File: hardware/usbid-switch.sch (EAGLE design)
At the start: 5 parts, among them J1 USB-MICRO-ZX80-B-5S, J2 USB-MICRO-105133-0011, SW1 SWITCH-SPDT-EG1215

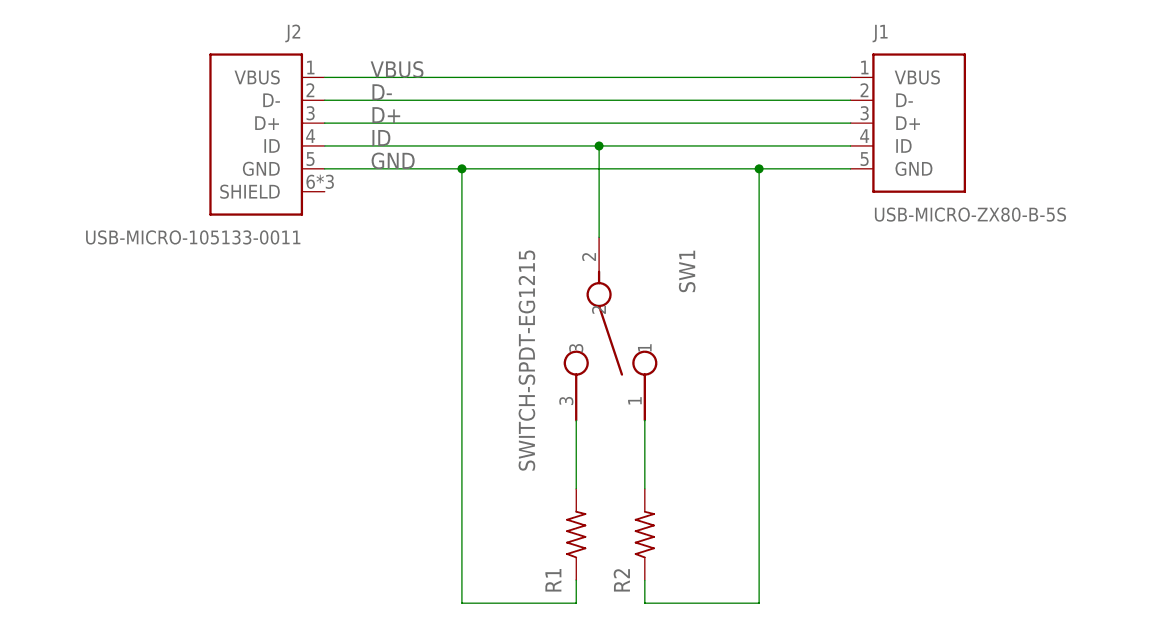
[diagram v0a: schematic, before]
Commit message: Updated BOM attributes for currently available parts
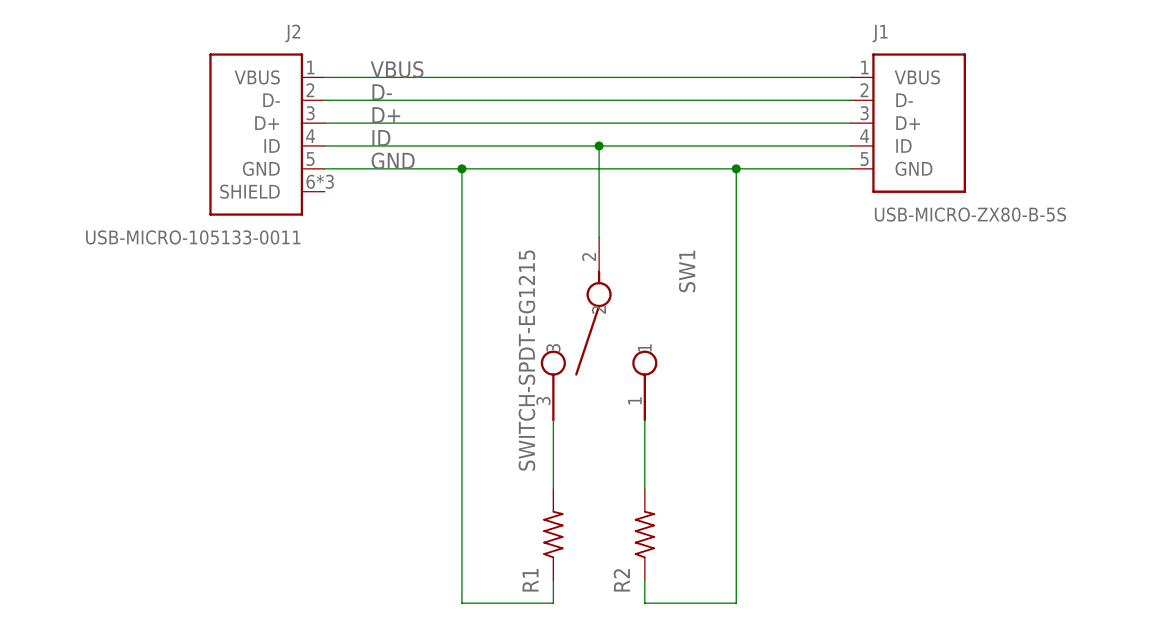
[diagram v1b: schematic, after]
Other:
- moved on the sheet: R1, SW1
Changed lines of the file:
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@@
 <?xml version="1.0" encoding="utf-8"?>
 <!DOCTYPE eagle SYSTEM "eagle.dtd">
-<eagle version="9.1.0">
+<eagle version="9.2.0">
 <drawing>
 <settings>
@@
 <setting verticaltext="up"/>
 </settings>
-<grid distance="0.1" unitdist="inch" unit="inch" style="lines" multiple="1" display="no" altdistance="0.01" altunitdist="inch" altunit="inch"/>
+<grid distance="0.1" unitdist="inch" unit="inch" style="dots" multiple="1" display="yes" altdistance="0.01" altunitdist="inch" altunit="inch"/>
 <layers>
 <layer number="1" name="Top" color="4" fill="1" visible="no" active="no"/>
@@
 <instance part="FRAME1" gate="G$1" x="0" y="0"/>
 <instance part="FRAME1" gate="G$2" x="135.89" y="3.81">
-<attribute name="SECTION" x="135.89" y="3.81" size="1.778" layer="96" display="off"/>
-</instance>
-<instance part="SW1" gate="G$1" x="88.9" y="129.54" rot="R270"/>
-<instance part="J1" gate="G$1" x="124.46" y="147.32"/>
-<instance part="J2" gate="G$1" x="50.8" y="144.78" rot="MR0"/>
-<instance part="R1" gate="G$1" x="86.36" y="101.6" smashed="yes" rot="R90">
-<attribute name="NAME" x="83.82" y="96.52" size="1.778" layer="95" rot="R90" align="center"/>
-<attribute name="VALUE" x="83.82" y="101.6" size="1.778" layer="96" rot="R90" align="center"/>
-</instance>
-<instance part="R2" gate="G$1" x="93.98" y="101.6" smashed="yes" rot="R90">
+<attribute name="LAST_DATE_TIME" x="199.39" y="31.75" size="2.54" layer="94" align="center-left"/>
+<attribute name="SHEET" x="242.57" y="6.35" size="2.54" layer="94" align="center-left"/>
+<attribute name="DRAWING_NAME" x="199.39" y="25.4" size="2.54" layer="94" align="center-left"/>
+<attribute name="REV" x="242.57" y="31.75" size="2.54" layer="94" align="center-left"/>
+<attribute name="DRAWING_NUM" x="199.39" y="11.43" size="2.54" layer="94" align="center-left"/>
+<attribute name="AUTHOR" x="161.29" y="16.51" size="2.54" layer="94" align="center"/>
+<attribute name="CONTACT_COMPANY" x="161.29" y="31.75" size="1.778" layer="94" align="center"/>
+<attribute name="CONTACT_ADDRESS" x="161.29" y="29.21" size="1.778" layer="94" align="center"/>
+<attribute name="CONTACT_PHONE" x="161.29" y="26.67" size="1.778" layer="94" align="center"/>
+<attribute name="SECTION" x="199.39" y="17.78" size="2.54" layer="94" align="center-left"/>
+</instance>
+<instance part="SW1" gate="G$1" x="88.9" y="129.54" rot="R270">
+<attribute name="NAME" x="97.797009375" y="133.353" size="1.7794" layer="95" rot="R270"/>
+<attribute name="VALUE" x="79.98855" y="133.3592" size="1.782290625" layer="96" rot="R270"/>
+</instance>
+<instance part="J1" gate="G$1" x="124.46" y="147.32">
+<attribute name="NAME" x="119.38" y="157.48" size="1.524" layer="95" align="center-left"/>
+<attribute name="VALUE" x="119.38" y="137.16" size="1.524" layer="96" align="center-left"/>
+</instance>
+<instance part="J2" gate="G$1" x="50.8" y="144.78" rot="MR0">
+<attribute name="NAME" x="55.88" y="157.48" size="1.524" layer="95" rot="MR0" align="center-left"/>
+<attribute name="VALUE" x="55.88" y="134.62" size="1.524" layer="96" rot="MR0" align="center-left"/>
+</instance>
+<instance part="R1" gate="G$1" x="83.82" y="101.6" rot="R90">
+<attribute name="NAME" x="81.28" y="96.52" size="1.778" layer="95" rot="R90" align="center"/>
+<attribute name="VALUE" x="81.28" y="101.6" size="1.778" layer="96" rot="R90" align="center"/>
+</instance>
+<instance part="R2" gate="G$1" x="93.98" y="101.6" rot="R90">
 <attribute name="NAME" x="91.44" y="96.52" size="1.778" layer="95" rot="R90" align="center"/>
 <attribute name="VALUE" x="91.44" y="101.6" size="1.778" layer="96" rot="R90" align="center"/>
@@
 <wire x1="58.42" y1="142.24" x2="73.66" y2="142.24" width="0.1524" layer="91"/>
 <pinref part="R2" gate="G$1" pin="1"/>
-<wire x1="73.66" y1="142.24" x2="106.68" y2="142.24" width="0.1524" layer="91"/>
-<wire x1="106.68" y1="142.24" x2="116.84" y2="142.24" width="0.1524" layer="91"/>
+<wire x1="73.66" y1="142.24" x2="104.14" y2="142.24" width="0.1524" layer="91"/>
+<wire x1="104.14" y1="142.24" x2="116.84" y2="142.24" width="0.1524" layer="91"/>
 <wire x1="93.98" y1="96.52" x2="93.98" y2="93.98" width="0.1524" layer="91"/>
-<wire x1="93.98" y1="93.98" x2="106.68" y2="93.98" width="0.1524" layer="91"/>
-<wire x1="106.68" y1="93.98" x2="106.68" y2="142.24" width="0.1524" layer="91"/>
-<junction x="106.68" y="142.24"/>
+<wire x1="93.98" y1="93.98" x2="104.14" y2="93.98" width="0.1524" layer="91"/>
+<wire x1="104.14" y1="93.98" x2="104.14" y2="142.24" width="0.1524" layer="91"/>
+<junction x="104.14" y="142.24"/>
 <pinref part="R1" gate="G$1" pin="1"/>
-<wire x1="86.36" y1="96.52" x2="86.36" y2="93.98" width="0.1524" layer="91"/>
-<wire x1="86.36" y1="93.98" x2="73.66" y2="93.98" width="0.1524" layer="91"/>
+<wire x1="83.82" y1="96.52" x2="83.82" y2="93.98" width="0.1524" layer="91"/>
+<wire x1="83.82" y1="93.98" x2="73.66" y2="93.98" width="0.1524" layer="91"/>
 <wire x1="73.66" y1="93.98" x2="73.66" y2="142.24" width="0.1524" layer="91"/>
 <junction x="73.66" y="142.24"/>
@@
 <pinref part="SW1" gate="G$1" pin="3"/>
 <pinref part="R1" gate="G$1" pin="2"/>
-<wire x1="86.36" y1="114.3" x2="86.36" y2="106.68" width="0.1524" layer="91"/>
-</segment>
-</net>
+<wire x1="83.82" y1="114.3" x2="83.82" y2="106.68" width="0.1524" layer="91"/>
+</segment>
+</net>
